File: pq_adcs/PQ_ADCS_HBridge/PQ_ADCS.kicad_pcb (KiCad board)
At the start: 6 copper layers, 40 x 40 mm, 62 parts, among them J1 CES-110-02-L-S, J10 Pico-Clasp_01x09, J11 Pico-Clasp_01x15, J12 CES-102-02-L-S, J2 CES-110-02-L-S, J3 CES-110-02-L-S, J4 CES-110-02-L-S, J5 Pico-Clasp_01x03, J6 Pico-Clasp_01x10, J7 Pico-Clasp_01x10, J8 Pico-Clasp_01x10, J9 Pico-Clasp_01x10, U1 LPV542, U2 LPV542, U3 LPV542, U4 IIM-42652, U5 DRV8214RTER, U6 TMUX1108RSVR, U7 MMC5983MA, U8 DRV8214RTER, U9 DRV8214RTER

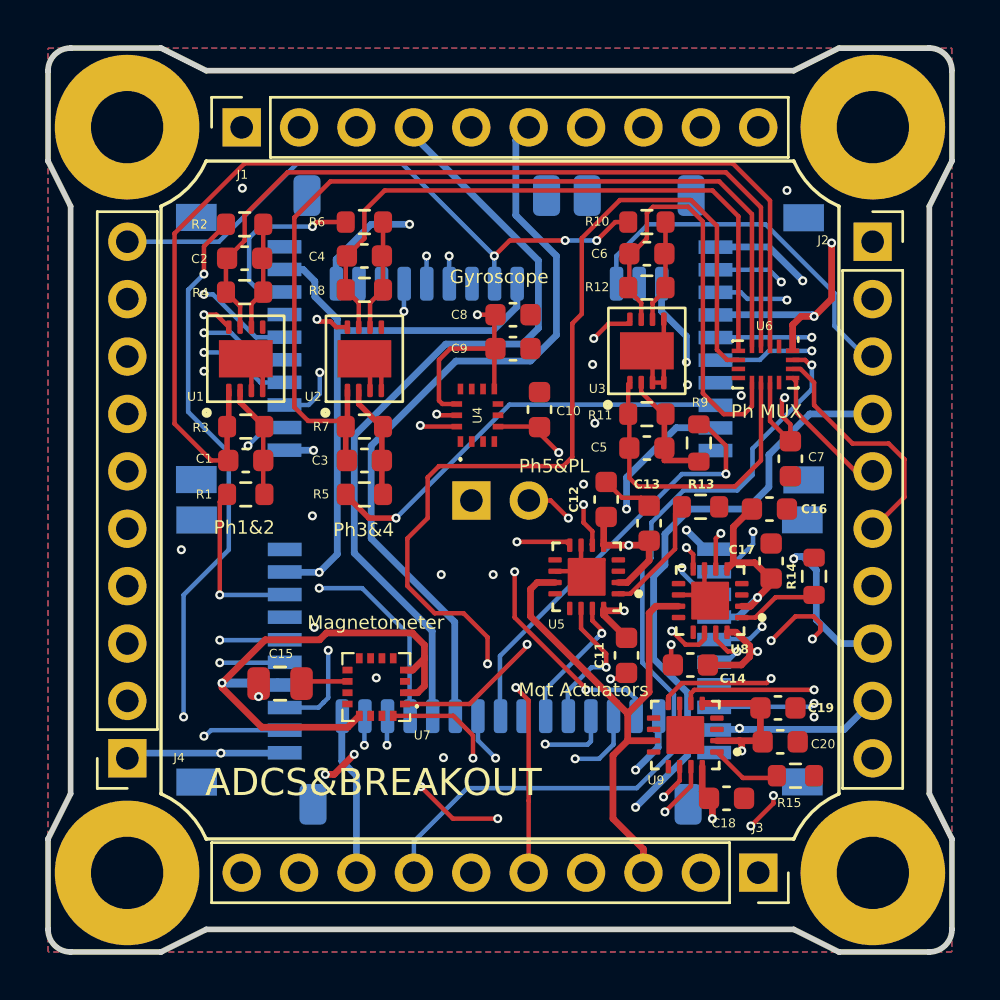
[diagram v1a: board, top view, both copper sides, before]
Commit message: ADCS corrected and verified. Production ready
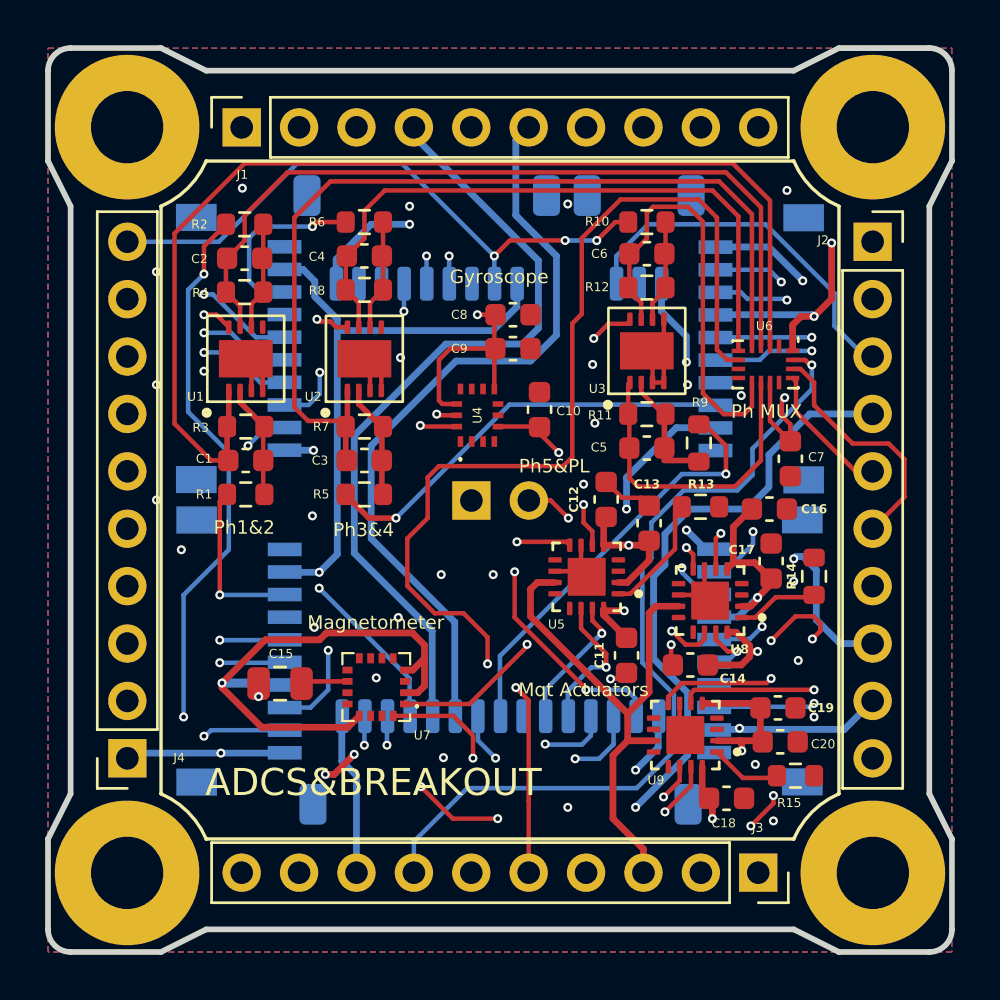
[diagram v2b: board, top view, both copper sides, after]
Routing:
- net 3V3_PERM: track 96.1 -> 105.3 mm
- net NRST: track 18.2 -> 17.1 mm
- net GND: vias 19 -> 31
